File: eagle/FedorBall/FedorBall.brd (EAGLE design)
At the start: 100 x 80 mm, 4 parts, among them IC1 MEGA16-P

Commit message: eagle scheme scratch
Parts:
- removed SV1, SV2: (no value), con-lstb:MA05-2
- added C4: (no value), rcl:C050-024X044
- added C5: 100n, rcl:C050-024X044
- added C6: 0.33u, rcl:C050-024X044
- added C7: 0.1u, rcl:C050-024X044
- added C8: 47u, rcl:C050-024X044
- added IC2: 7805T, linear:TO220H
- added JP1, JP2: M05X2SHD, SparkFun:2X5-SHROUDED
- added R1, R2, R3, R4: 10k, rcl:0207/10
- added X1, X2: 22-23-2041, con-molex:22-23-2041
- S1: device SparkFun:TACTILE-PTH -> SparkFun:KSA_SEALED_TAC_SWITCH
- moved IC1 89.9 mm to (43.2, 45.7), flipped to the bottom, turned to 270 degrees
- moved S1 75.2 mm to (27.9, 8.89)
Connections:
- removed net AVCC: IC1.30
- new net +5V: C7.1, C8.1, IC1.10, IC1.30, IC2.3, JP1.2, R1.2
- new net N$10: IC1.34
- new net N$11: IC1.35
- new net N$12: IC1.36
- new net N$13: IC1.37
- new net N$14: IC1.38
- new net N$15: IC1.39
- new net N$16: IC1.40
- new net N$2: C5.1, IC1.32
- new net N$5: IC1.6, JP1.1, R4.2
- new net N$6: C4.1, IC1.9, JP1.5, R1.1, S1.P$3
- new net N$7: IC1.8, JP1.7, R2.2
- new net N$8: IC1.7, JP1.9, R3.2
- new net N$9: IC1.33
- net GND: now also C4.2, C5.2, C6.2, C7.2, C8.2, IC2.2, JP1.10, JP1.8, S1.P$1
- net VCC: now also C6.1, IC2.1; no longer IC1.10

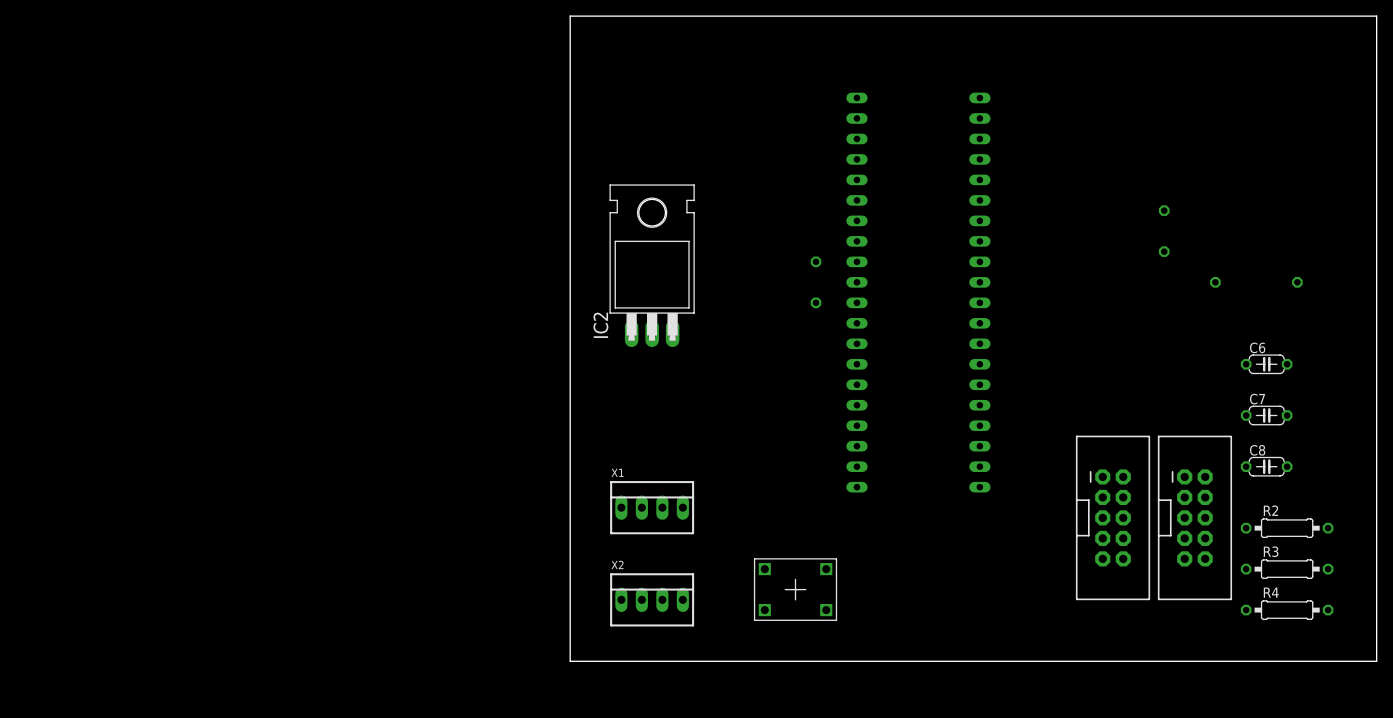
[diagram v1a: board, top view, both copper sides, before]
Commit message: update main scheme and board
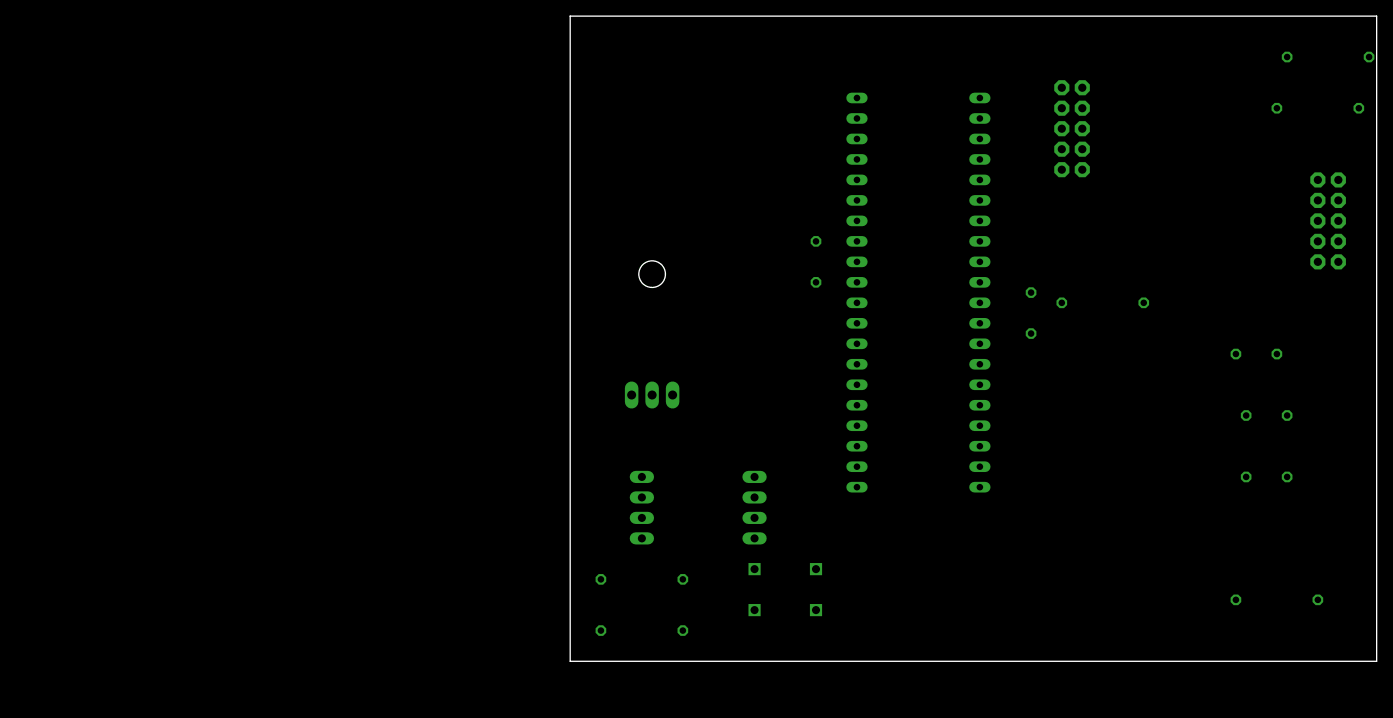
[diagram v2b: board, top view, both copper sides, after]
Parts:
- removed JP1, JP2: M05X2SHD, SparkFun:2X5-SHROUDED
- added LED_DRIVER, SPI: M05X2SHD, SparkFun:2X5-SHROUDED
- added R5, R6: 10k, rcl:0207/10
- moved R2 58.6 mm to (94.0, 74.9), flipped to the bottom
- moved R3 57.3 mm to (92.7, 68.6), flipped to the bottom
- moved C4 19.4 mm to (57.1, 43.2)
- moved R1 19.2 mm to (66.0, 44.5)
- moved X2 17.1 mm to (22.9, 19.1), flipped to the bottom, turned to 90 degrees
- moved IC2 7.62 mm to (10.2, 43.2), flipped to the bottom
- moved C5 2.54 mm to (30.5, 49.5)
- moved R4 1.80 mm to (87.6, 7.62), flipped to the bottom
- moved C6 1.80 mm to (85.1, 38.1), flipped to the bottom, turned to 180 degrees
- moved C8 1.27 mm to (86.4, 22.9), flipped to the bottom, turned to 180 degrees
- moved S1 1.27 mm to (26.7, 8.89), flipped to the bottom
- moved X1 1.27 mm to (8.89, 19.1), flipped to the bottom, turned to 90 degrees
- flipped C7 to the bottom, turned to 180 degrees
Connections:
- new net BLANK: IC1.3, LED_DRIVER.2
- new net GSCLK: IC1.4, LED_DRIVER.4
- new net IN1: X1.4
- new net IN2: X1.3
- new net MISO: LED_DRIVER.3, R3.1
- new net MOSI: LED_DRIVER.5, R4.1
- new net SCK: LED_DRIVER.1, R2.1
- new net SCL: IC1.22, R6.2, X2.1
- new net SDA: IC1.23, R5.2, X2.2
- new net SDO: X2.3
- new net VPRG: IC1.2, LED_DRIVER.6
- new net XLAT: IC1.5, LED_DRIVER.7
- net +5V: now also LED_DRIVER.10, LED_DRIVER.8, R5.1, R6.1, SPI.2, X1.1, X2.4; no longer JP1.2
- net GND: now also LED_DRIVER.9, SPI.10, SPI.8, X1.2; no longer JP1.10, JP1.8
- net N$5: now also SPI.1; no longer JP1.1
- net N$6: now also SPI.5; no longer JP1.5
- net N$7: now also SPI.7; no longer JP1.7
- net N$8: now also SPI.9; no longer JP1.9

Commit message: schematic tweaks
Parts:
- C4: value (none) -> 10u
- C5: value 100n -> 0.1u
- R1: value 10k -> 100k
- renumbered SPI to ISP
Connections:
- removed net IN1: X1.4
- removed net IN2: X1.3
- new net INT0: IC1.17, X1.4
- new net INT1: IC1.16, X1.3
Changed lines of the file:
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@@
 <attribute name="OC_FARNELL" value="9171142" x="53.34" y="6.35" size="1.778" layer="28" rot="MR270" display="off"/>
 </element>
-<element name="C4" library="rcl" package="C050-024X044" value="" x="57.15" y="43.18" rot="MR270"/>
-<element name="C5" library="rcl" package="C050-024X044" value="100n" x="30.48" y="49.53" rot="MR270"/>
-<element name="R1" library="rcl" package="0207/10" value="10k" x="66.04" y="44.45" rot="MR180"/>
+<element name="C4" library="rcl" package="C050-024X044" value="10u" x="57.15" y="43.18" rot="MR270"/>
+<element name="C5" library="rcl" package="C050-024X044" value="0.1u" x="30.48" y="49.53" rot="MR270"/>
+<element name="R1" library="rcl" package="0207/10" value="100k" x="66.04" y="44.45" rot="MR180"/>
 <element name="S1" library="SparkFun" package="KSA_SEALED_TAC_SWITCH" value="" x="26.67" y="8.89" rot="MR0"/>
 <element name="IC2" library="linear" package="TO220H" value="7805T" x="10.16" y="43.18" rot="MR0"/>
@@
 <element name="R3" library="rcl" package="0207/10" value="10k" x="92.71" y="68.58" rot="MR0"/>
 <element name="R4" library="rcl" package="0207/10" value="10k" x="87.63" y="7.62" rot="MR0"/>
-<element name="SPI" library="SparkFun" package="2X5-SHROUDED" value="M05X2SHD" x="62.23" y="66.04" rot="MR180"/>
+<element name="ISP" library="SparkFun" package="2X5-SHROUDED" value="M05X2SHD" x="62.23" y="66.04" rot="MR180"/>
 <element name="LED_DRIVER" library="SparkFun" package="2X5-SHROUDED" value="M05X2SHD" x="93.98" y="54.61" rot="MR180"/>
 <element name="R5" library="rcl" package="0207/10" value="10k" x="8.89" y="10.16" rot="MR180"/>
@@
 <contactref element="IC1" pad="30"/>
 <contactref element="IC1" pad="10"/>
-<contactref element="SPI" pad="2"/>
+<contactref element="ISP" pad="2"/>
 <contactref element="C8" pad="1"/>
 <contactref element="IC2" pad="3"/>
@@
 <contactref element="IC1" pad="11"/>
 <contactref element="S1" pad="P$1"/>
-<contactref element="SPI" pad="10"/>
-<contactref element="SPI" pad="8"/>
+<contactref element="ISP" pad="10"/>
+<contactref element="ISP" pad="8"/>
 <contactref element="IC2" pad="2"/>
 <contactref element="C6" pad="2"/>
@@
 <contactref element="IC1" pad="6"/>
 <contactref element="R4" pad="2"/>
-<contactref element="SPI" pad="1"/>
+<contactref element="ISP" pad="1"/>
 <wire x1="82.55" y1="7.62" x2="60.96" y2="60.96" width="0" layer="19" extent="1-1"/>
 <wire x1="50.8" y1="57.15" x2="60.96" y2="60.96" width="0" layer="19" extent="1-1"/>
@@
 <contactref element="IC1" pad="8"/>
 <contactref element="R2" pad="2"/>
-<contactref element="SPI" pad="7"/>
+<contactref element="ISP" pad="7"/>
 <wire x1="88.9" y1="74.93" x2="60.96" y2="68.58" width="0" layer="19" extent="1-1"/>
 <wire x1="50.8" y1="52.07" x2="88.9" y2="74.93" width="0" layer="19" extent="1-1"/>
@@
 <contactref element="IC1" pad="7"/>
 <contactref element="R3" pad="2"/>
-<contactref element="SPI" pad="9"/>
+<contactref element="ISP" pad="9"/>
 <wire x1="87.63" y1="68.58" x2="60.96" y2="71.12" width="0" layer="19" extent="1-1"/>
 <wire x1="50.8" y1="54.61" x2="87.63" y2="68.58" width="0" layer="19" extent="1-1"/>
@@
 <contactref element="IC1" pad="9"/>
 <contactref element="S1" pad="P$3"/>
-<contactref element="SPI" pad="5"/>
+<contactref element="ISP" pad="5"/>
 <wire x1="60.96" y1="44.45" x2="57.15" y2="45.72" width="0" layer="19" extent="1-1"/>
 <wire x1="50.8" y1="49.53" x2="57.15" y2="45.72" width="0" layer="19" extent="1-1"/>
@@
 <signal name="N$16">
 <contactref element="IC1" pad="40"/>
-</signal>
-<signal name="VCC">
-<contactref element="IC2" pad="1"/>
-<contactref element="C6" pad="1"/>
-<wire x1="12.7" y1="33.02" x2="82.55" y2="38.1" width="0" layer="19" extent="1-1"/>
-</signal>
-<signal name="IN2">
-<contactref element="X1" pad="3"/>
-</signal>
-<signal name="IN1">
-<contactref element="X1" pad="4"/>
 </signal>
 <signal name="SCL">
@@
 <wire x1="92.71" y1="57.15" x2="50.8" y2="59.69" width="0" layer="19" extent="1-1"/>
 </signal>
+<signal name="VCC">
+<contactref element="IC2" pad="1"/>
+<contactref element="C6" pad="1"/>
+<wire x1="12.7" y1="33.02" x2="82.55" y2="38.1" width="0" layer="19" extent="1-1"/>
+</signal>
+<signal name="INT1">
+<contactref element="IC1" pad="16"/>
+<contactref element="X1" pad="3"/>
+<wire x1="8.89" y1="20.32" x2="50.8" y2="31.75" width="0" layer="19" extent="1-1"/>
+</signal>
+<signal name="INT0">
+<contactref element="IC1" pad="17"/>
+<contactref element="X1" pad="4"/>
+<wire x1="8.89" y1="22.86" x2="50.8" y2="29.21" width="0" layer="19" extent="1-1"/>
+</signal>
 </signals>

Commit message: update scheme
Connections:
- removed net MISO: LED_DRIVER.3, R3.1
- removed net MOSI: LED_DRIVER.5, R4.1
- removed net SCK: LED_DRIVER.1, R2.1
- new net MISO_10K: LED_DRIVER.8, R3.1
- new net MOSI_10K: LED_DRIVER.9, R4.1
- new net SCK_10K: LED_DRIVER.10, R2.1
- net +5V: now also LED_DRIVER.2, LED_DRIVER.4; no longer LED_DRIVER.10, LED_DRIVER.8
- net BLANK: now also LED_DRIVER.6; no longer LED_DRIVER.2
- net GND: now also ISP.6, LED_DRIVER.1; no longer LED_DRIVER.9
- net GSCLK: now also LED_DRIVER.7; no longer LED_DRIVER.4
- net VPRG: now also LED_DRIVER.5; no longer LED_DRIVER.6
- net XLAT: now also LED_DRIVER.3; no longer LED_DRIVER.7
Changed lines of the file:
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@@
 <contactref element="R6" pad="1"/>
 <contactref element="X1" pad="1"/>
-<contactref element="LED_DRIVER" pad="10"/>
-<contactref element="LED_DRIVER" pad="8"/>
 <contactref element="X2" pad="4"/>
-<wire x1="95.25" y1="57.15" x2="95.25" y2="59.69" width="0" layer="19" extent="1-1"/>
-<wire x1="71.12" y1="44.45" x2="95.25" y2="57.15" width="0" layer="19" extent="1-1"/>
+<contactref element="LED_DRIVER" pad="2"/>
+<contactref element="LED_DRIVER" pad="4"/>
+<wire x1="95.25" y1="49.53" x2="95.25" y2="52.07" width="0" layer="19" extent="1-1"/>
+<wire x1="83.82" y1="30.48" x2="95.25" y2="49.53" width="0" layer="19" extent="1-1"/>
+<wire x1="83.82" y1="22.86" x2="83.82" y2="30.48" width="0" layer="19" extent="1-1"/>
+<wire x1="71.12" y1="44.45" x2="83.82" y2="30.48" width="0" layer="19" extent="1-1"/>
 <wire x1="63.5" y1="60.96" x2="71.12" y2="44.45" width="0" layer="19" extent="1-1"/>
-<wire x1="83.82" y1="30.48" x2="71.12" y2="44.45" width="0" layer="19" extent="1-1"/>
-<wire x1="83.82" y1="22.86" x2="83.82" y2="30.48" width="0" layer="19" extent="1-1"/>
 <wire x1="50.8" y1="46.99" x2="63.5" y2="60.96" width="0" layer="19" extent="1-1"/>
 <wire x1="35.56" y1="44.45" x2="50.8" y2="46.99" width="0" layer="19" extent="1-1"/>
-<wire x1="7.62" y1="33.02" x2="35.56" y2="44.45" width="0" layer="19" extent="1-1"/>
-<wire x1="8.89" y1="15.24" x2="7.62" y2="33.02" width="0" layer="19" extent="1-1"/>
+<wire x1="22.86" y1="22.86" x2="35.56" y2="44.45" width="0" layer="19" extent="1-1"/>
+<wire x1="8.89" y1="15.24" x2="22.86" y2="22.86" width="0" layer="19" extent="1-1"/>
 <wire x1="3.81" y1="10.16" x2="8.89" y2="15.24" width="0" layer="19" extent="1-1"/>
 <wire x1="3.81" y1="3.81" x2="3.81" y2="10.16" width="0" layer="19" extent="1-1"/>
-<wire x1="22.86" y1="22.86" x2="8.89" y2="15.24" width="0" layer="19" extent="1-1"/>
+<wire x1="7.62" y1="33.02" x2="8.89" y2="15.24" width="0" layer="19" extent="1-1"/>
 </signal>
 <signal name="GND">
@@
 <contactref element="C8" pad="2"/>
 <contactref element="X1" pad="2"/>
-<contactref element="LED_DRIVER" pad="9"/>
-<wire x1="87.63" y1="38.1" x2="57.15" y2="40.64" width="0" layer="19" extent="1-1"/>
+<contactref element="LED_DRIVER" pad="1"/>
+<contactref element="ISP" pad="6"/>
+<wire x1="87.63" y1="38.1" x2="92.71" y2="49.53" width="0" layer="19" extent="1-1"/>
 <wire x1="88.9" y1="30.48" x2="87.63" y2="38.1" width="0" layer="19" extent="1-1"/>
 <wire x1="88.9" y1="22.86" x2="88.9" y2="30.48" width="0" layer="19" extent="1-1"/>
-<wire x1="63.5" y1="68.58" x2="88.9" y2="22.86" width="0" layer="19" extent="1-1"/>
-<wire x1="63.5" y1="71.12" x2="63.5" y2="68.58" width="0" layer="19" extent="1-1"/>
-<wire x1="92.71" y1="59.69" x2="63.5" y2="71.12" width="0" layer="19" extent="1-1"/>
+<wire x1="57.15" y1="40.64" x2="87.63" y2="38.1" width="0" layer="19" extent="1-1"/>
 <wire x1="50.8" y1="44.45" x2="57.15" y2="40.64" width="0" layer="19" extent="1-1"/>
 <wire x1="35.56" y1="46.99" x2="50.8" y2="44.45" width="0" layer="19" extent="1-1"/>
@@
 <wire x1="8.89" y1="17.78" x2="10.16" y2="33.02" width="0" layer="19" extent="1-1"/>
 <wire x1="30.48" y1="11.43" x2="8.89" y2="17.78" width="0" layer="19" extent="1-1"/>
+<wire x1="63.5" y1="66.04" x2="50.8" y2="44.45" width="0" layer="19" extent="1-1"/>
+<wire x1="63.5" y1="68.58" x2="63.5" y2="66.04" width="0" layer="19" extent="1-1"/>
+<wire x1="63.5" y1="71.12" x2="63.5" y2="68.58" width="0" layer="19" extent="1-1"/>
 </signal>
 <signal name="N$2">
@@
 <contactref element="X2" pad="3"/>
 </signal>
-<signal name="SCK">
-<contactref element="R2" pad="1"/>
-<contactref element="LED_DRIVER" pad="1"/>
-<wire x1="92.71" y1="49.53" x2="99.06" y2="74.93" width="0" layer="19" extent="1-1"/>
-</signal>
-<signal name="MISO">
-<contactref element="R3" pad="1"/>
-<contactref element="LED_DRIVER" pad="3"/>
-<wire x1="92.71" y1="52.07" x2="97.79" y2="68.58" width="0" layer="19" extent="1-1"/>
-</signal>
-<signal name="MOSI">
-<contactref element="R4" pad="1"/>
-<contactref element="LED_DRIVER" pad="5"/>
-<wire x1="92.71" y1="54.61" x2="92.71" y2="7.62" width="0" layer="19" extent="1-1"/>
-</signal>
 <signal name="BLANK">
-<contactref element="LED_DRIVER" pad="2"/>
 <contactref element="IC1" pad="3"/>
-<wire x1="95.25" y1="49.53" x2="50.8" y2="64.77" width="0" layer="19" extent="1-1"/>
+<contactref element="LED_DRIVER" pad="6"/>
+<wire x1="50.8" y1="64.77" x2="95.25" y2="54.61" width="0" layer="19" extent="1-1"/>
 </signal>
 <signal name="GSCLK">
-<contactref element="LED_DRIVER" pad="4"/>
 <contactref element="IC1" pad="4"/>
-<wire x1="95.25" y1="52.07" x2="50.8" y2="62.23" width="0" layer="19" extent="1-1"/>
+<contactref element="LED_DRIVER" pad="7"/>
+<wire x1="50.8" y1="62.23" x2="92.71" y2="57.15" width="0" layer="19" extent="1-1"/>
 </signal>
 <signal name="VPRG">
-<contactref element="LED_DRIVER" pad="6"/>
 <contactref element="IC1" pad="2"/>
-<wire x1="95.25" y1="54.61" x2="50.8" y2="67.31" width="0" layer="19" extent="1-1"/>
-</signal>
-<signal name="XLAT">
-<contactref element="LED_DRIVER" pad="7"/>
-<contactref element="IC1" pad="5"/>
-<wire x1="92.71" y1="57.15" x2="50.8" y2="59.69" width="0" layer="19" extent="1-1"/>
+<contactref element="LED_DRIVER" pad="5"/>
+<wire x1="50.8" y1="67.31" x2="92.71" y2="54.61" width="0" layer="19" extent="1-1"/>
 </signal>
 <signal name="VCC">
@@
 <wire x1="8.89" y1="22.86" x2="50.8" y2="29.21" width="0" layer="19" extent="1-1"/>
 </signal>
+<signal name="XLAT">
+<contactref element="IC1" pad="5"/>
+<contactref element="LED_DRIVER" pad="3"/>
+<wire x1="50.8" y1="59.69" x2="92.71" y2="52.07" width="0" layer="19" extent="1-1"/>
+</signal>
+<signal name="SCK_10K">
+<contactref element="R2" pad="1"/>
+<contactref element="LED_DRIVER" pad="10"/>
+<wire x1="95.25" y1="59.69" x2="99.06" y2="74.93" width="0" layer="19" extent="1-1"/>
+</signal>
+<signal name="MISO_10K">
+<contactref element="R3" pad="1"/>
+<contactref element="LED_DRIVER" pad="8"/>
+<wire x1="95.25" y1="57.15" x2="97.79" y2="68.58" width="0" layer="19" extent="1-1"/>
+</signal>
+<signal name="MOSI_10K">
+<contactref element="R4" pad="1"/>
+<contactref element="LED_DRIVER" pad="9"/>
+<wire x1="92.71" y1="7.62" x2="92.71" y2="59.69" width="0" layer="19" extent="1-1"/>
+</signal>
 </signals>

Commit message: update schematic for main board
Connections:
- net BLANK: now also IC1.18; no longer IC1.3
- net GSCLK: now also IC1.21; no longer IC1.4
- net VPRG: now also IC1.20; no longer IC1.2
- net XLAT: now also IC1.19; no longer IC1.5
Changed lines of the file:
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@@
 </signal>
 <signal name="BLANK">
-<contactref element="IC1" pad="3"/>
 <contactref element="LED_DRIVER" pad="6"/>
-<wire x1="50.8" y1="64.77" x2="95.25" y2="54.61" width="0" layer="19" extent="1-1"/>
+<contactref element="IC1" pad="18"/>
+<wire x1="50.8" y1="26.67" x2="95.25" y2="54.61" width="0" layer="19" extent="1-1"/>
 </signal>
 <signal name="GSCLK">
-<contactref element="IC1" pad="4"/>
 <contactref element="LED_DRIVER" pad="7"/>
-<wire x1="50.8" y1="62.23" x2="92.71" y2="57.15" width="0" layer="19" extent="1-1"/>
+<contactref element="IC1" pad="21"/>
+<wire x1="35.56" y1="21.59" x2="92.71" y2="57.15" width="0" layer="19" extent="1-1"/>
 </signal>
 <signal name="VPRG">
-<contactref element="IC1" pad="2"/>
 <contactref element="LED_DRIVER" pad="5"/>
-<wire x1="50.8" y1="67.31" x2="92.71" y2="54.61" width="0" layer="19" extent="1-1"/>
+<contactref element="IC1" pad="20"/>
+<wire x1="50.8" y1="21.59" x2="92.71" y2="54.61" width="0" layer="19" extent="1-1"/>
 </signal>
 <signal name="VCC">
@@
 </signal>
 <signal name="XLAT">
-<contactref element="IC1" pad="5"/>
 <contactref element="LED_DRIVER" pad="3"/>
-<wire x1="50.8" y1="59.69" x2="92.71" y2="52.07" width="0" layer="19" extent="1-1"/>
+<contactref element="IC1" pad="19"/>
+<wire x1="50.8" y1="24.13" x2="92.71" y2="52.07" width="0" layer="19" extent="1-1"/>
 </signal>
 <signal name="SCK_10K">
